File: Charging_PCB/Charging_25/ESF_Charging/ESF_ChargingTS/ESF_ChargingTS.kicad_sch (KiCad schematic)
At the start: 12 parts, among them J1 Insulation_Monitoring_Device, J2 Conn_02x03_Counter_Clockwise, J3 Conn_02x03_Counter_Clockwise, K1 G2RL-1, K2 G2RL-1

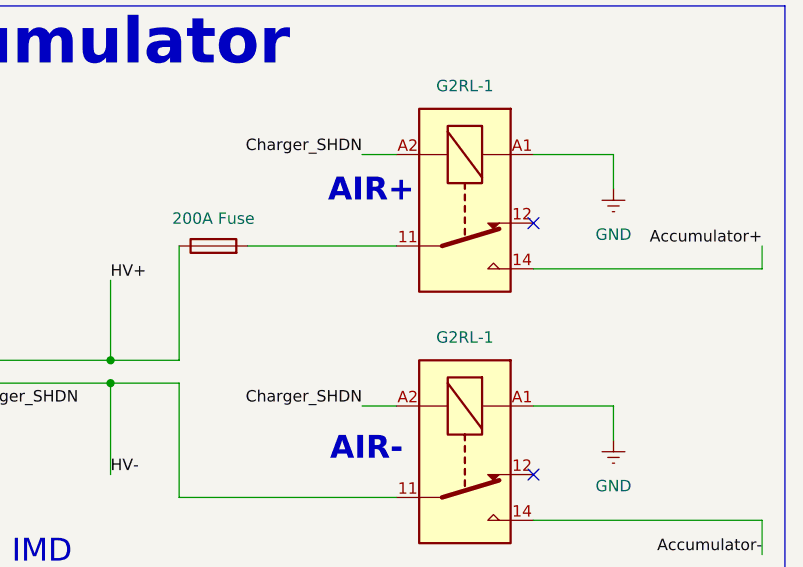
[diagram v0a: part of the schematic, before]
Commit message: charging pcb layout
charging pcb ready to order, would like funny logo on there
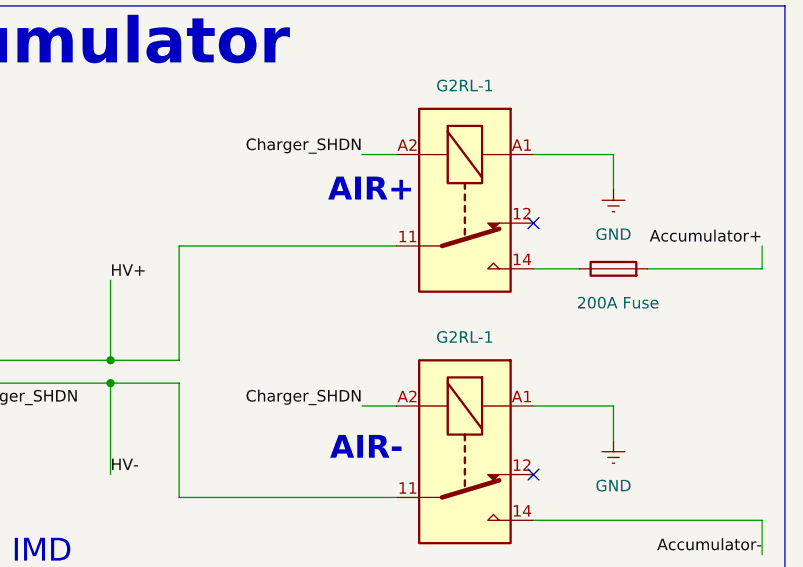
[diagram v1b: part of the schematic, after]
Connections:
- net Accumulator+: now also F1.2; no longer K1.14
- net HV+: now also K1.11; no longer F1.1
- new net: F1.1, K1.14
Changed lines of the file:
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@@
+	(wire
+		(pts
+			(xy 204.47 88.9) (xy 204.47 76.2)
+		)
+		(stroke
+			(width 0)
+			(type default)
+			(color 255 153 0 1)
+		)
+	)
 	(wire
 		(pts
@@
 	(wire
 		(pts
-			(xy 269.24 78.74) (xy 243.84 78.74)
-		)
-		(stroke
-			(width 0)
-			(type default)
-			(color 255 153 0 1)
-		)
-	)
-	(wire
-		(pts
-			(xy 212.09 76.2) (xy 228.6 76.2)
-		)
-		(stroke
-			(width 0)
-			(type default)
-			(color 255 153 0 1)
-		)
-	)
-	(wire
-		(pts
 			(xy 33.02 106.68) (xy 33.02 99.06)
 		)
@@
 	(wire
 		(pts
+			(xy 256.54 78.74) (xy 269.24 78.74)
+		)
+		(stroke
+			(width 0)
+			(type default)
+			(color 255 153 0 1)
+		)
+	)
+	(wire
+		(pts
 			(xy 182.88 121.92) (xy 180.34 121.92)
 		)
@@
 	(wire
 		(pts
-			(xy 204.47 76.2) (xy 204.47 88.9)
-		)
-		(stroke
-			(width 0)
-			(type default)
-			(color 255 153 0 1)
-		)
-	)
-	(wire
-		(pts
 			(xy 36.83 106.68) (xy 36.83 101.6)
 		)
@@
 	(wire
 		(pts
+			(xy 204.47 76.2) (xy 228.6 76.2)
+		)
+		(stroke
+			(width 0)
+			(type default)
+			(color 255 153 0 1)
+		)
+	)
+	(wire
+		(pts
 			(xy 196.85 88.9) (xy 204.47 88.9)
 		)
@@
 			(type default)
 			(color 0 255 255 1)
+		)
+	)
+	(wire
+		(pts
+			(xy 243.84 78.74) (xy 248.92 78.74)
+		)
+		(stroke
+			(width 0)
+			(type default)
+			(color 255 153 0 1)
 		)
 	)
@@
 	(symbol
 		(lib_id "Device:Fuse")
-		(at 208.28 76.2 90)
+		(at 252.73 78.74 90)
 		(unit 1)
 		(exclude_from_sim no)
@@
 		(dnp no)
 		(property "Reference" "F1"
-			(at 208.28 69.85 90)
+			(at 252.73 72.39 90)
 			(effects
 				(font
@@
 		)
 		(property "Value" "200A Fuse"
-			(at 208.28 73.152 90)
+			(at 253.238 82.55 90)
 			(effects
 				(font
@@
 		)
 		(property "Footprint" ""
-			(at 208.28 77.978 90)
+			(at 252.73 80.518 90)
 			(effects
 				(font
@@
 		)
 		(property "Datasheet" "~"
-			(at 208.28 76.2 0)
+			(at 252.73 78.74 0)
 			(effects
 				(font
@@
 		)
 		(property "Description" "Fuse"
-			(at 208.28 76.2 0)
-			(effects
-				(font
+			(at 252.73 78.74 0)
+			(effects
+				(font

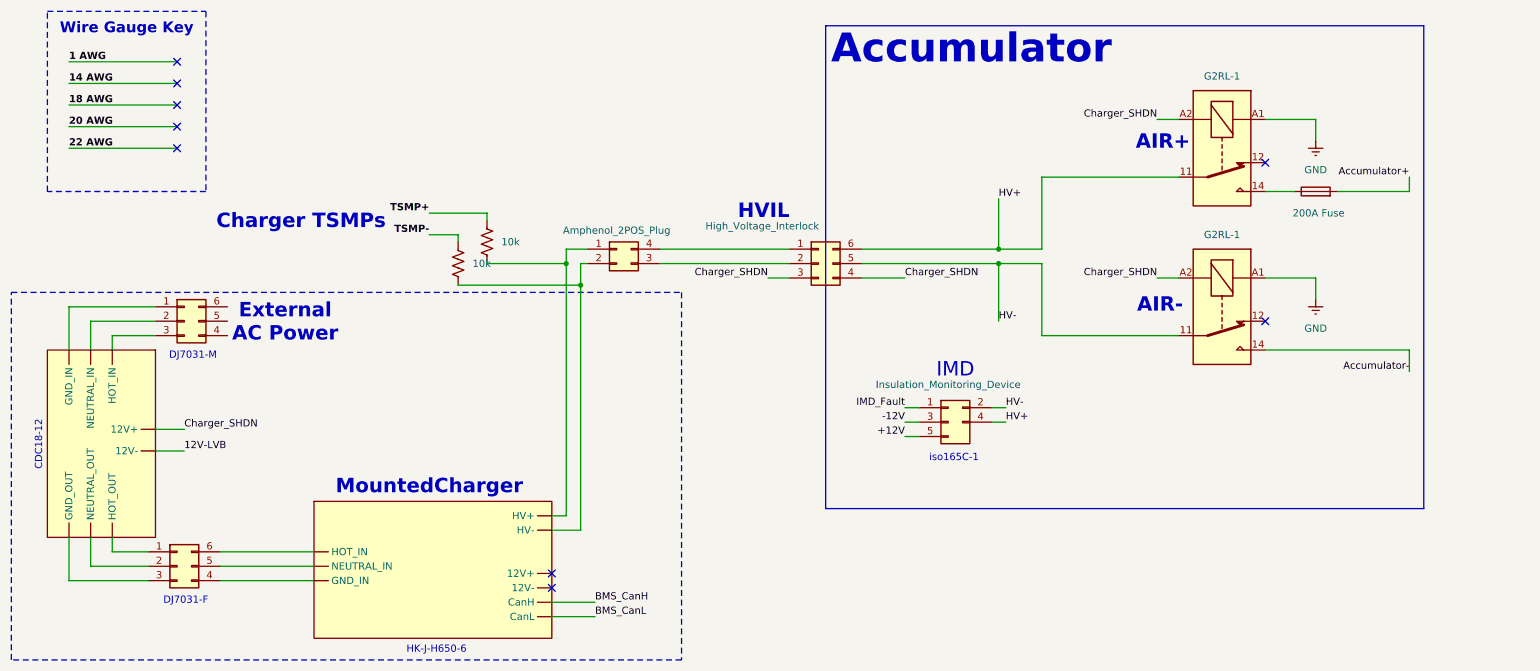
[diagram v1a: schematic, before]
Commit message: started TS schematic
TS schematic for ESF
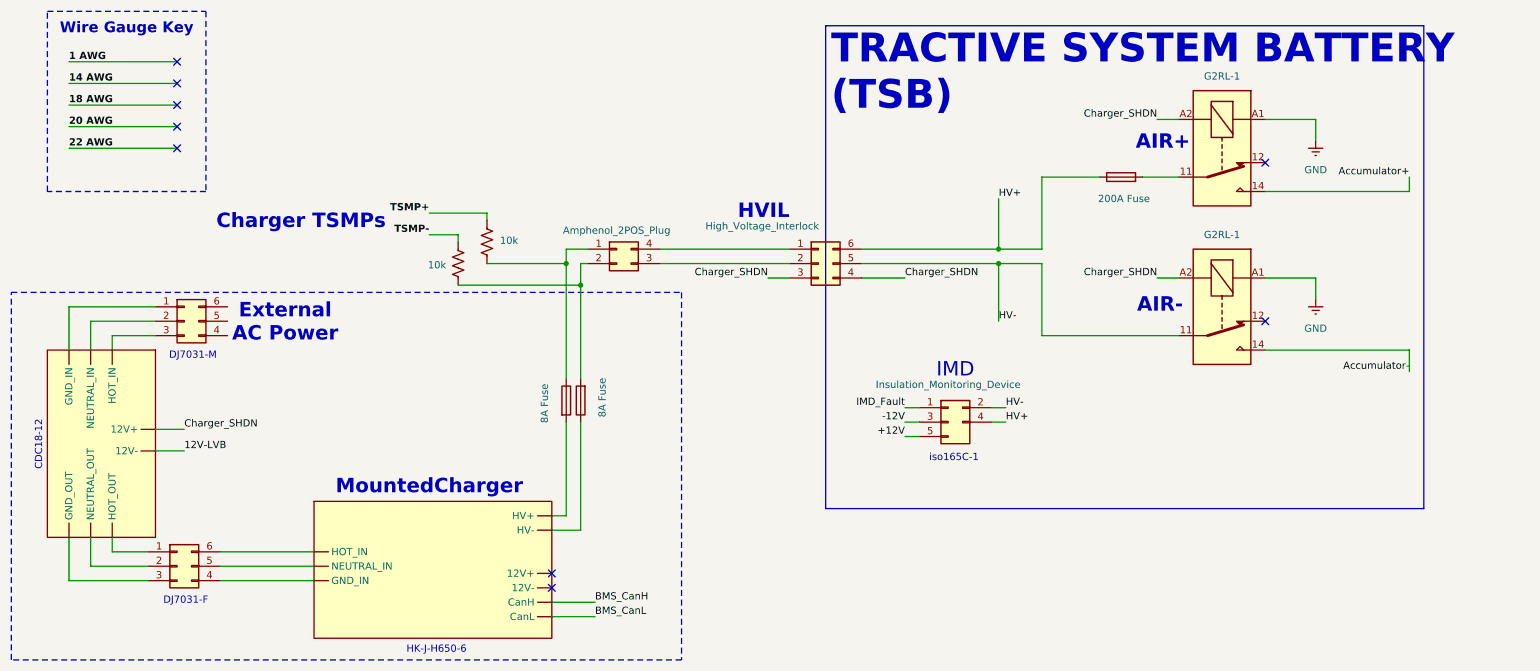
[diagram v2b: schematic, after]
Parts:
- added F2, F3: 8A Fuse, symbol Device:Fuse
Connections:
- net Accumulator+: now also K1.14; no longer F1.2
- net HV+: now also F1.1; no longer K1.11
- net at 10k.2, Amphenol_2POS_Plug.1 (Pin_1): now also F2.1; no longer U1. (CanL)
- net at 10k.2, Amphenol_2POS_Plug.2 (Pin_2): now also F3.2; no longer U1. (CanL)
- new net: F3.1, U1. (CanL)
- new net: F2.2, U1. (CanL)
- new net: F1.2, K1.11
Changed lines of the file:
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@@
 		)
 	)
-	(text_box "Accumulator"
+	(text_box "TRACTIVE SYSTEM BATTERY (TSB)"
 		(exclude_from_sim no)
 		(at 166.37 49.53 0)
@@
 	)
 	(junction
-		(at 123.19 95.25)
+		(at 196.85 91.44)
 		(diameter 0)
 		(color 0 0 0 0)
 	)
 	(junction
-		(at 196.85 91.44)
+		(at 123.19 95.25)
 		(diameter 0)
 		(color 0 0 0 0)
@@
 	(wire
 		(pts
-			(xy 256.54 78.74) (xy 269.24 78.74)
-		)
-		(stroke
-			(width 0)
-			(type default)
-			(color 255 153 0 1)
-		)
-	)
-	(wire
-		(pts
 			(xy 182.88 121.92) (xy 180.34 121.92)
 		)
@@
 	(wire
 		(pts
+			(xy 120.65 119.38) (xy 120.65 135.89)
+		)
+		(stroke
+			(width 0)
+			(type default)
+			(color 255 153 0 1)
+		)
+	)
+	(wire
+		(pts
+			(xy 123.19 119.38) (xy 123.19 138.43)
+		)
+		(stroke
+			(width 0)
+			(type default)
+			(color 255 153 0 1)
+		)
+	)
+	(wire
+		(pts
 			(xy 182.88 116.84) (xy 180.34 116.84)
 		)
@@
 	(wire
 		(pts
+			(xy 243.84 78.74) (xy 269.24 78.74)
+		)
+		(stroke
+			(width 0)
+			(type default)
+			(color 255 153 0 1)
+		)
+	)
+	(wire
+		(pts
 			(xy 101.6 95.25) (xy 123.19 95.25)
 		)
@@
 	(wire
 		(pts
-			(xy 204.47 76.2) (xy 228.6 76.2)
-		)
-		(stroke
-			(width 0)
-			(type default)
-			(color 255 153 0 1)
-		)
-	)
-	(wire
-		(pts
 			(xy 196.85 88.9) (xy 204.47 88.9)
 		)
@@
 	(wire
 		(pts
+			(xy 123.19 95.25) (xy 123.19 111.76)
+		)
+		(stroke
+			(width 0)
+			(type default)
+			(color 255 153 0 1)
+		)
+	)
+	(wire
+		(pts
 			(xy 106.68 91.44) (xy 120.65 91.44)
 		)
@@
 	(wire
 		(pts
+			(xy 222.25 76.2) (xy 228.6 76.2)
+		)
+		(stroke
+			(width 0)
+			(type default)
+			(color 255 153 0 1)
+		)
+	)
+	(wire
+		(pts
 			(xy 196.85 91.44) (xy 204.47 91.44)
 		)
@@
 	(wire
 		(pts
+			(xy 204.47 76.2) (xy 214.63 76.2)
+		)
+		(stroke
+			(width 0)
+			(type default)
+			(color 255 153 0 1)
+		)
+	)
+	(wire
+		(pts
 			(xy 182.88 119.38) (xy 180.34 119.38)
 		)
@@
 	(wire
 		(pts
-			(xy 243.84 78.74) (xy 248.92 78.74)
-		)
-		(stroke
-			(width 0)
-			(type default)
-			(color 255 153 0 1)
-		)
-	)
-	(wire
-		(pts
 			(xy 33.02 147.32) (xy 33.02 139.7)
 		)
@@
 	(wire
 		(pts
-			(xy 120.65 91.44) (xy 120.65 135.89)
-		)
-		(stroke
-			(width 0)
-			(type default)
-			(color 255 153 0 1)
-		)
-	)
-	(wire
-		(pts
 			(xy 33.02 59.69) (xy 52.07 59.69)
 		)
@@
 	(wire
 		(pts
-			(xy 123.19 95.25) (xy 123.19 138.43)
+			(xy 120.65 91.44) (xy 120.65 111.76)
 		)
 		(stroke
@@
 			)
 			(justify right bottom)
+		)
+	)
+	(symbol
+		(lib_id "Device:Fuse")
+		(at 123.19 115.57 180)
+		(unit 1)
+		(exclude_from_sim no)
+		(in_bom yes)
+		(on_board yes)
+		(dnp no)
+		(property "Reference" "F3"
+			(at 116.84 115.57 90)
+			(effects
+				(font
+					(size 1.27 1.27)
+				)
+				(hide yes)
+			)
+		)
+		(property "Value" "8A Fuse"
+			(at 127 115.062 90)
+			(effects
+				(font
+					(size 1.27 1.27)
+				)
+			)
+		)
+		(property "Footprint" ""
+			(at 124.968 115.57 90)
+			(effects
+				(font
+					(size 1.27 1.27)
+				)
+				(hide yes)
+			)
+		)
+		(property "Datasheet" "~"
+			(at 123.19 115.57 0)
+			(effects
+				(font
+					(size 1.27 1.27)
+				)
+				(hide yes)
+			)
+		)
+		(property "Description" "Fuse"
+			(at 123.19 115.57 0)
+			(effects
+				(font
+					(size 1.27 1.27)
+				)
+				(hide yes)
+			)
+		)
+		(pin "1"
+		)
+		(pin "2"
+		)
+		(instances
+			(project "ESF_ChargingTS"
+				(path "/19554fd2-0239-4caa-8cb4-b38f2c8d5e09"
+					(reference "F3")
+					(unit 1)
+				)
+			)
 		)
 	)
@@
 		(on_board yes)
 		(dnp no)
-		(fields_autoplaced yes)
 		(property "Reference" "10k"
-			(at 109.22 87.6299 0)
+			(at 108.966 87.376 0)
 			(effects
 				(font
@@
 		(on_board yes)
 		(dnp no)
-		(fields_autoplaced yes)
 		(property "Reference" "10k"
-			(at 104.14 91.4399 0)
+			(at 96.266 91.694 0)
 			(effects
 				(font
@@
 	(symbol
 		(lib_id "Device:Fuse")
-		(at 252.73 78.74 90)
+		(at 120.65 115.57 0)
+		(unit 1)
+		(exclude_from_sim no)
+		(in_bom yes)
+		(on_board yes)
+		(dnp no)
+		(property "Reference" "F2"
+			(at 127 115.57 90)
+			(effects
+				(font
+					(size 1.27 1.27)
+				)
+				(hide yes)
+			)
+		)
+		(property "Value" "8A Fuse"
+			(at 116.84 116.078 90)
+			(effects
+				(font
+					(size 1.27 1.27)
+				)
+			)
+		)
+		(property "Footprint" ""
+			(at 118.872 115.57 90)
+			(effects
+				(font
+					(size 1.27 1.27)
+				)
+				(hide yes)
+			)
+		)
+		(property "Datasheet" "~"
+			(at 120.65 115.57 0)
+			(effects
+				(font
+					(size 1.27 1.27)
+				)
+				(hide yes)
+			)
+		)
+		(property "Description" "Fuse"
+			(at 120.65 115.57 0)
+			(effects
+				(font
+					(size 1.27 1.27)
+				)
+				(hide yes)
+			)
+		)
+		(pin "1"
+		)
+		(pin "2"
+		)
+		(instances
+			(project "ESF_ChargingTS"
+				(path "/19554fd2-0239-4caa-8cb4-b38f2c8d5e09"
+					(reference "F2")
+					(unit 1)
+				)
+			)
+		)
+	)
+	(symbol
+		(lib_id "Device:Fuse")
+		(at 218.44 76.2 90)
 		(unit 1)
 		(exclude_from_sim no)
@@
 		(dnp no)
 		(property "Reference" "F1"
-			(at 252.73 72.39 90)
+			(at 218.44 69.85 90)
 			(effects
 				(font
@@
 		)
 		(property "Value" "200A Fuse"
-			(at 253.238 82.55 90)
+			(at 218.948 80.01 90)
 			(effects
 				(font
@@
 		)
 		(property "Footprint" ""
-			(at 252.73 80.518 90)
+			(at 218.44 77.978 90)
 			(effects
 				(font
@@
 		)
 		(property "Datasheet" "~"
-			(at 252.73 78.74 0)
+			(at 218.44 76.2 0)
 			(effects
 				(font
@@
 		)
 		(property "Description" "Fuse"
-			(at 252.73 78.74 0)
-			(effects
-				(font
+			(at 218.44 76.2 0)
+			(effects
+				(font
